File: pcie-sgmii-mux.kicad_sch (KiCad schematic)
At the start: 0 parts

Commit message: [#81876] Cleanup connections
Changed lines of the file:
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@@
-		)
-	)
-	(hierarchical_label "PCIE_x1{PCIE}"
-		(shape bidirectional)
-		(at 175.26 101.6 0)
-		(effects
-			(font
-				(size 1.27 1.27)
-			)
-			(justify left)
 		)
 	)

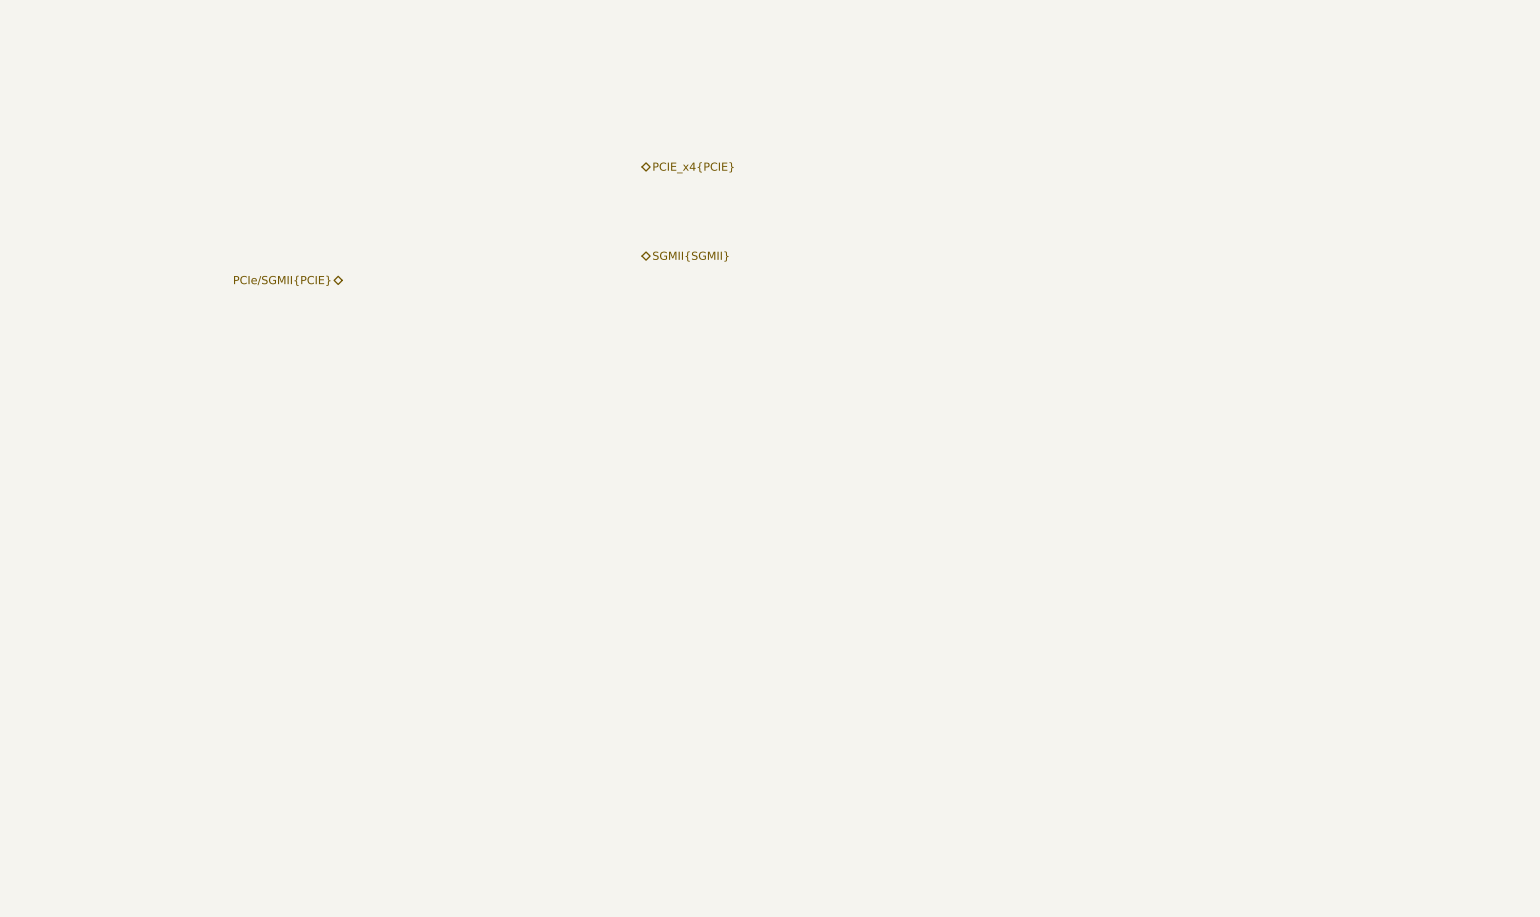
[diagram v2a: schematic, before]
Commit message: [#82226] Add PCIe/SGMII mux
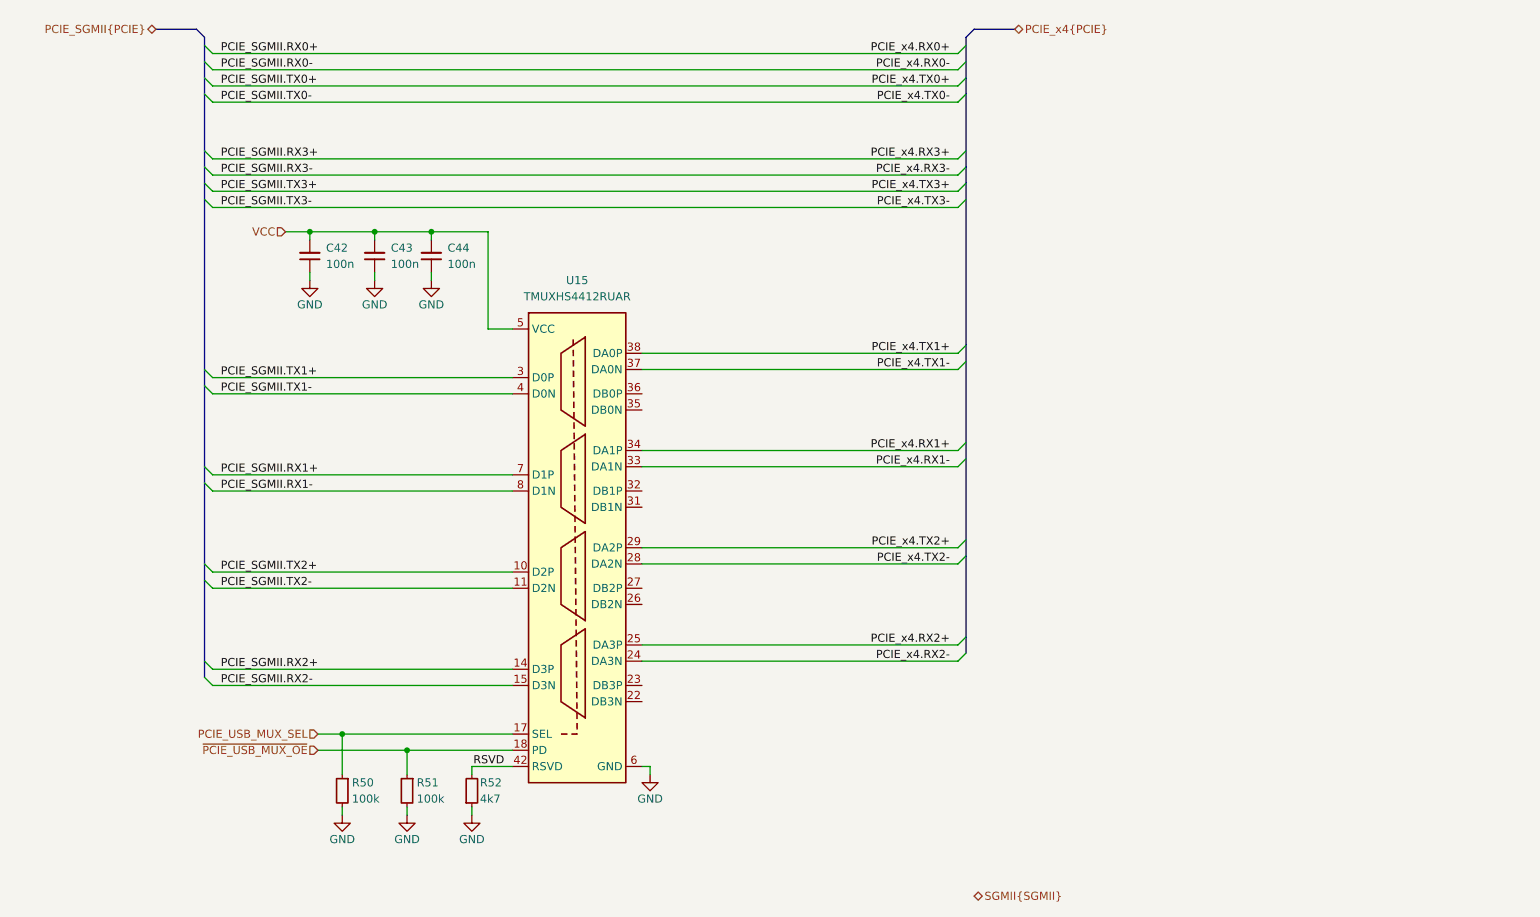
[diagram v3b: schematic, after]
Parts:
- added C42, C43, C44: C_100n_0402, antmicro-footprints:C_0402_1005Metric, symbol antmicroCapacitors0402:C_100n_0402
- added R50, R51: R_100k_0402, antmicro-footprints:R_0402_1005Metric, symbol antmicroResistors0402:R_100k_0402
- added R52: R_4k7_0402, antmicro-footprints:R_0402_1005Metric, symbol antmicroResistors0402:R_4k7_0402
- added U15: TMUXHS4412RUAR, antmicro-footprints:WQFN-42-1EP_3.5x9mm_P0.5mm, symbol antmicroInterfaceAnalogSwitchesSpecialPurpose:TMUXHS4412RUAR
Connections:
- new net GND: C42.1, C43.1, C44.1, R50.2, R51.2, R52.1, U15.16 (GND), U15.21 (GND), U15.30 (GND), U15.39 (GND), U15.43 (GND), U15.6 (GND), U15.9 (GND)
- new net PCIE_SGMII.RX1+: U15.7 (D1P)
- new net PCIE_SGMII.RX1-: U15.8 (D1N)
- new net PCIE_SGMII.RX2+: U15.14 (D3P)
- new net PCIE_SGMII.RX2-: U15.15 (D3N)
- new net PCIE_SGMII.TX1+: U15.3 (D0P)
- new net PCIE_SGMII.TX1-: U15.4 (D0N)
- new net PCIE_SGMII.TX2+: U15.10 (D2P)
- new net PCIE_SGMII.TX2-: U15.11 (D2N)
- new net PCIE_USB_MUX_SEL: R50.1, U15.17 (SEL)
- new net PCIE_x4.RX1+: U15.34 (DA1P)
- new net PCIE_x4.RX1-: U15.33 (DA1N)
- new net PCIE_x4.RX2+: U15.25 (DA3P)
- new net PCIE_x4.RX2-: U15.24 (DA3N)
- new net PCIE_x4.TX1+: U15.38 (DA0P)
- new net PCIE_x4.TX1-: U15.37 (DA0N)
- new net PCIE_x4.TX2+: U15.29 (DA2P)
- new net PCIE_x4.TX2-: U15.28 (DA2N)
- new net RSVD: R52.2, U15.42 (RSVD)
- new net VCC: C42.2, C43.2, C44.2, U15.13 (VCC), U15.5 (VCC)
- new net ~{PCIE_USB_MUX_OE}: R51.1, U15.18 (PD)

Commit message: Changed A4 sheets to A3 and cleaned them up
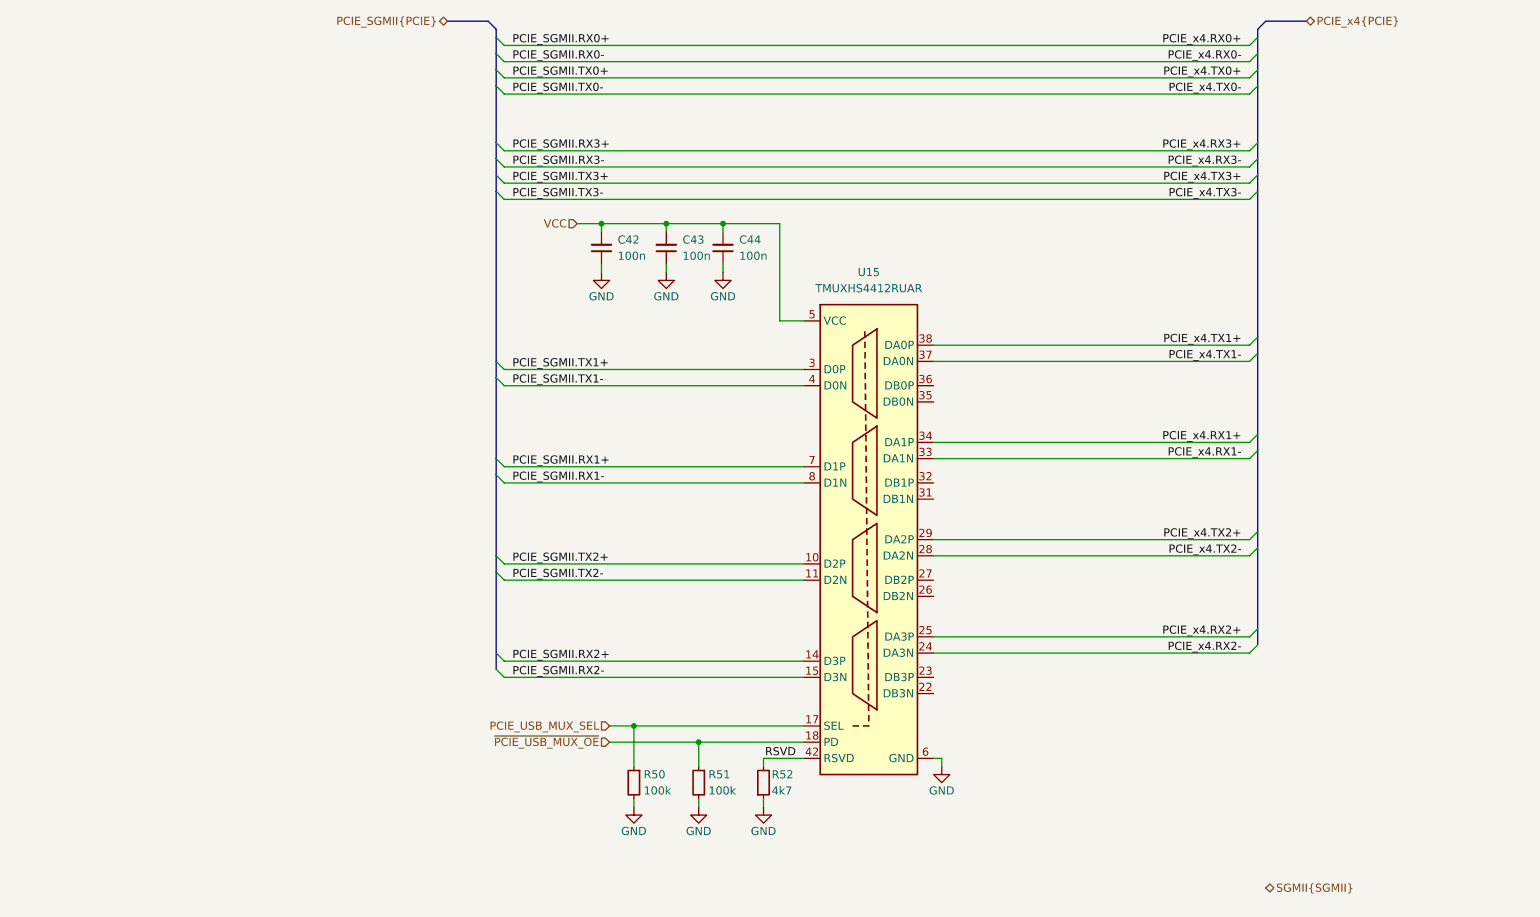
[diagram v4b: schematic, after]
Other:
- moved on the sheet: C42, C43, C44, R50, R51, R52, U15

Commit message: [#83337] Finalized PCIe-SGMII mux and PCIe-USB mux
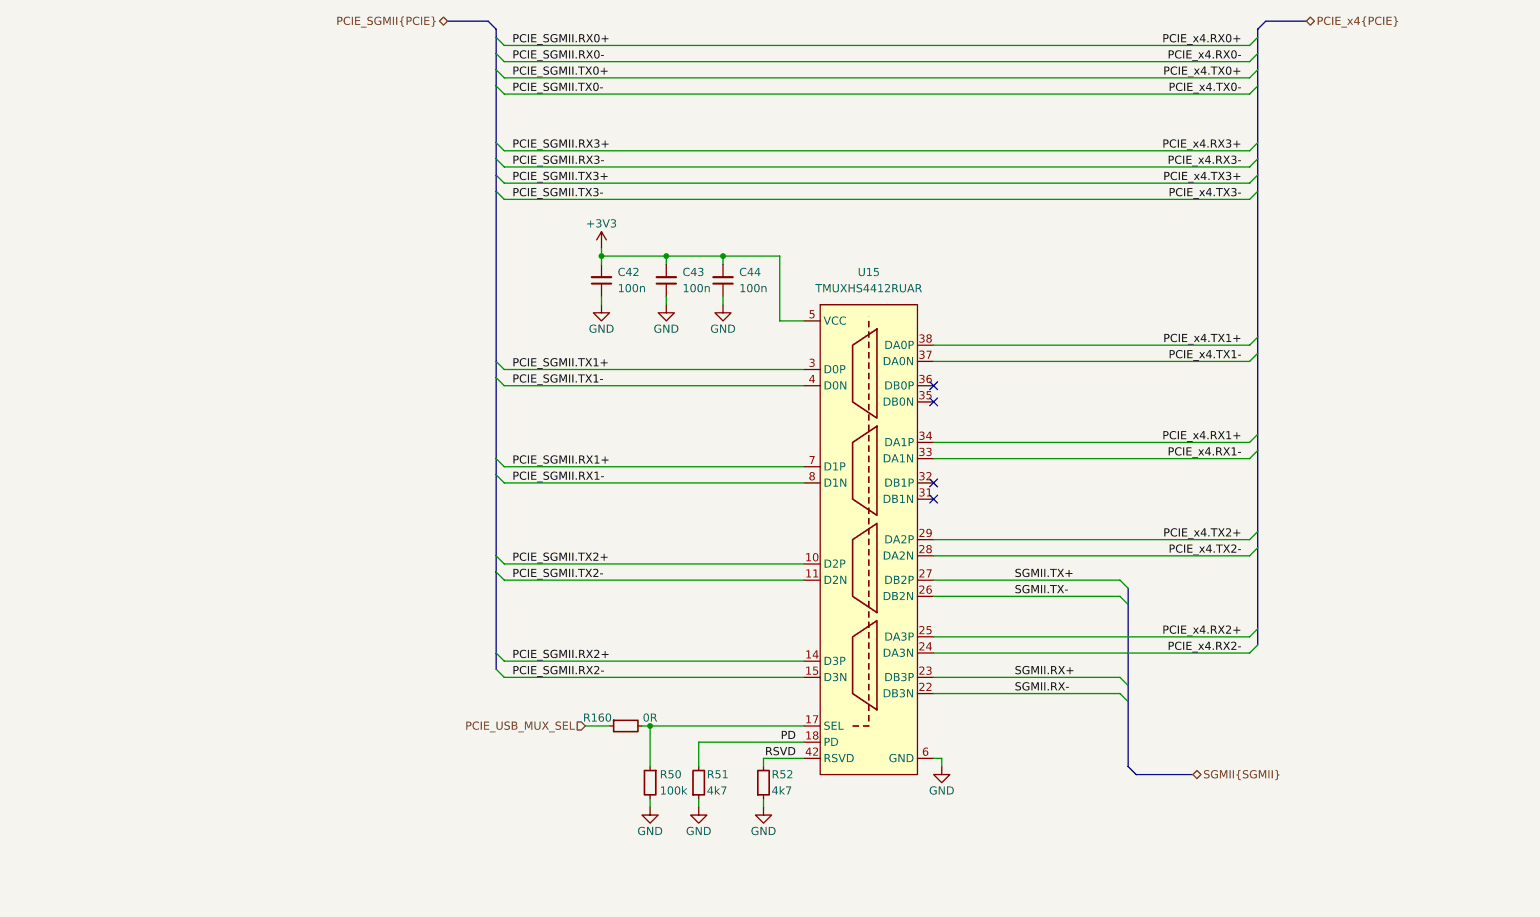
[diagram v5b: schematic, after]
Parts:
- removed R51: R_100k_0402, antmicro-footprints:R_0402_1005Metric, symbol antmicroResistors0402:R_100k_0402
- added R160: R_0R_0402, antmicro-footprints:R_0402_1005Metric, symbol antmicroResistors0402:R_0R_0402
- added R51: R_4k7_0402, antmicro-footprints:R_0402_1005Metric, symbol antmicroResistors0402:R_4k7_0402
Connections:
- net GND: now also R51.1
- net PCIE_USB_MUX_SEL: now also R160.1; no longer R50.1, U15.17 (SEL)
- net SGMII.RX-: now reaches U15.22 (DB3N)
- net SGMII.RX+: now reaches U15.23 (DB3P)
- net SGMII.TX-: now reaches U15.26 (DB2N)
- net SGMII.TX+: now reaches U15.27 (DB2P)
- net VCC renamed +3V3
- net ~{PCIE_USB_MUX_OE} renamed PD
- net PD: now also R51.2
- new net: R160.2, R50.1, U15.17 (SEL)
- no-connect marks 0 -> 4
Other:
- moved on the sheet: C42, C43, C44, R50

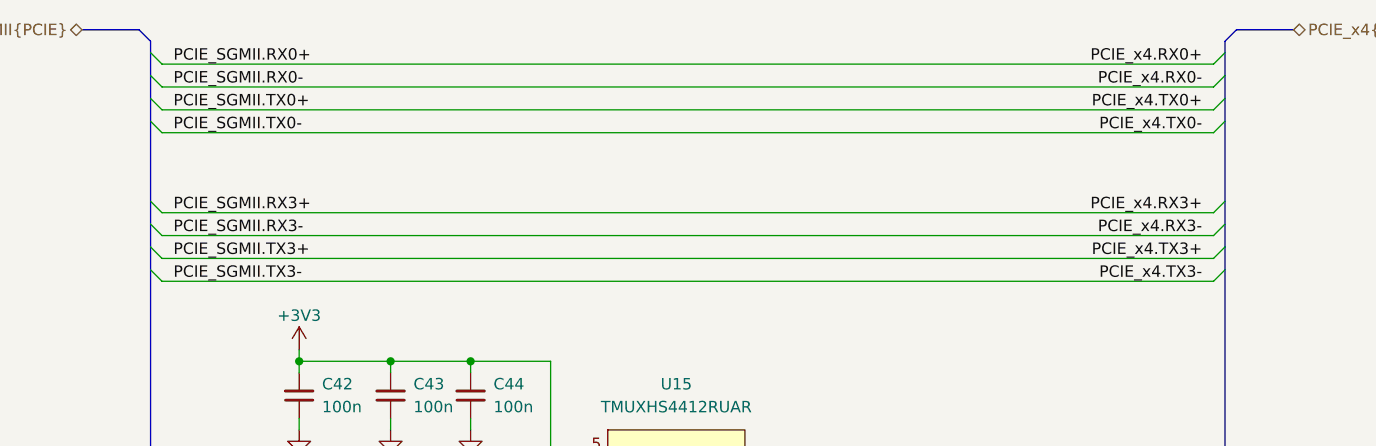
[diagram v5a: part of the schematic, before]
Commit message: [#83338] Low speed PCIe x4 connections
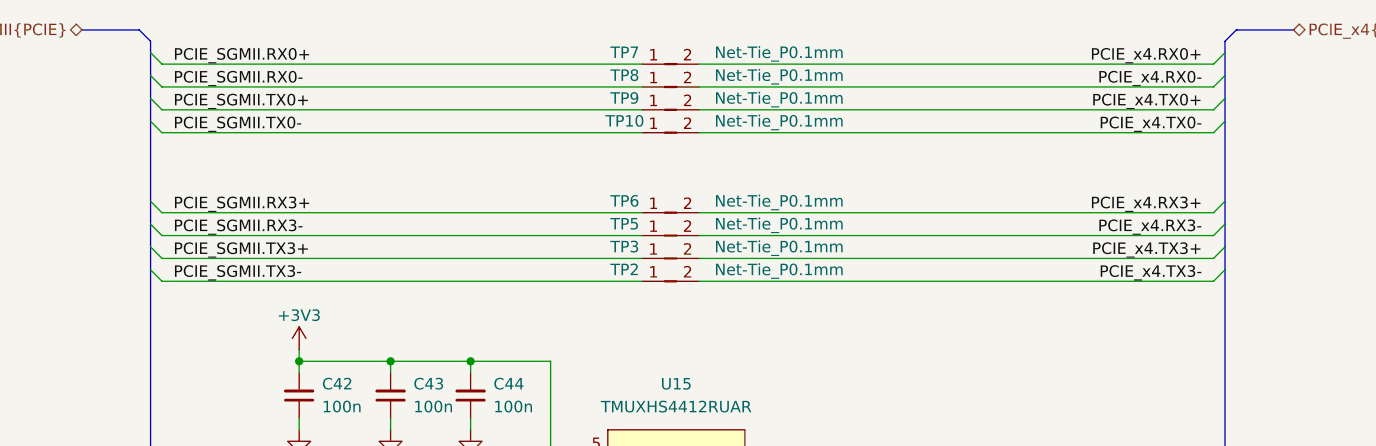
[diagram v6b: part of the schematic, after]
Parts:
- added TP10, TP2, TP3, TP5, TP6, TP7, TP8, TP9: Net-Tie_P0.1mm, antmicro-footprints:NetTie-2_SMD_Pad0.1mm, symbol antmicroShuntsJumpers:Net-Tie_P0.1mm
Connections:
- net PCIE_SGMII.RX0+: now also TP7.1
- net PCIE_SGMII.RX0-: now also TP8.1
- net PCIE_SGMII.RX3+: now also TP6.1
- net PCIE_SGMII.RX3-: now also TP5.1
- net PCIE_SGMII.TX0+: now also TP9.1
- net PCIE_SGMII.TX0-: now also TP10.1
- net PCIE_SGMII.TX3+: now also TP3.1
- net PCIE_SGMII.TX3-: now also TP2.1
- new net PCIE_x4.RX0+: TP7.2
- new net PCIE_x4.RX0-: TP8.2
- new net PCIE_x4.RX3+: TP6.2
- new net PCIE_x4.RX3-: TP5.2
- new net PCIE_x4.TX0+: TP9.2
- new net PCIE_x4.TX0-: TP10.2
- new net PCIE_x4.TX3+: TP3.2
- new net PCIE_x4.TX3-: TP2.2
